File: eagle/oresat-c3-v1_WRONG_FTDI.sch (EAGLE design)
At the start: 168 parts, among them J1 J-SAMTEC-TFM-110-X1-XXX-D-RA, J10 U.FL, J11 U.FL, J13 U.FL, J14 U.FL, J15 HARWIN-2X8X1.27, J19 HARWIN-2X8X1.27, J2 U.FL, J3 U.FL, J4 U.FL, J6 J-SAMTEC-TFM-120-X1-XXX-D-RA, J7 FTSH-105-XX-X-DV-K, J8 U.FL, J9 U.FL, Q1 MOSFET-PCH-SOT23-6, U1 MAX892LEUA+T21-0036K-L, U11 U-ONSEMI-AX5043, U12 LP2985XX-N, U13 U-ONSEMI-AX5043, U14 LP2985XX-N, U2 TCAN330, U3 TCAN330, U4 TPS259621 - eFuse, U5 TPS62111RSA, U6 MAX6374KA-T21-0078H-L, U7 STM32F446RE, U9 SFEM016GB1EM1TO-A-HG-111-STD, X1 16MHZ-2.5x2mm, X3 TAITIEN-TY, X4 TAITIEN-TY

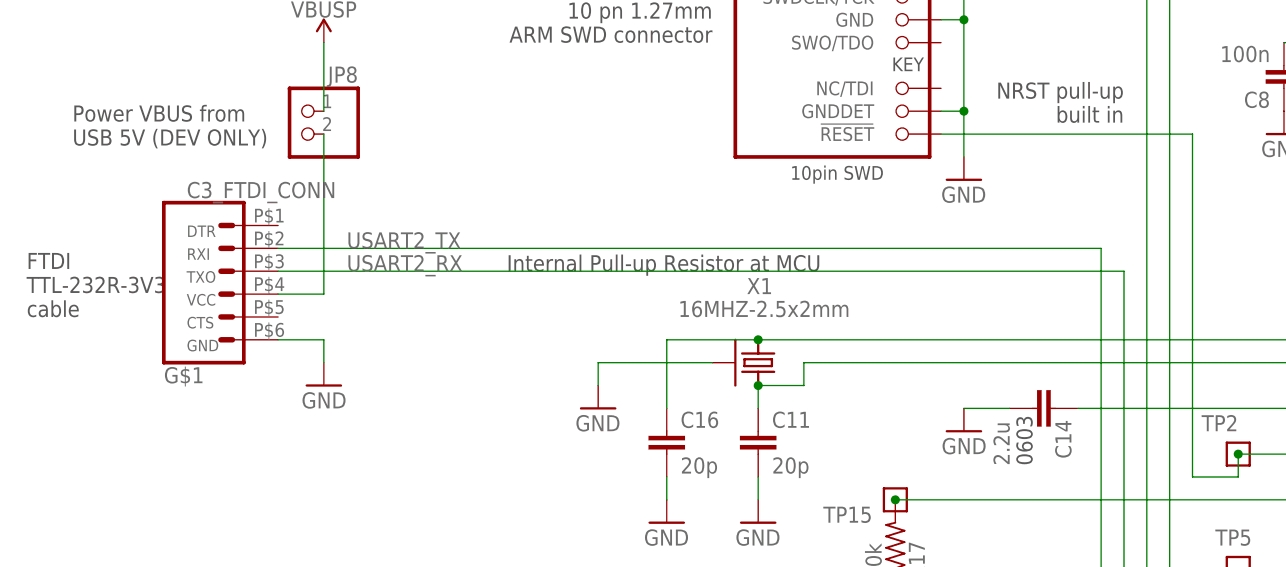
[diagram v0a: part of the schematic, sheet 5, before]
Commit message: switched the TX and RX pins to be the correct way
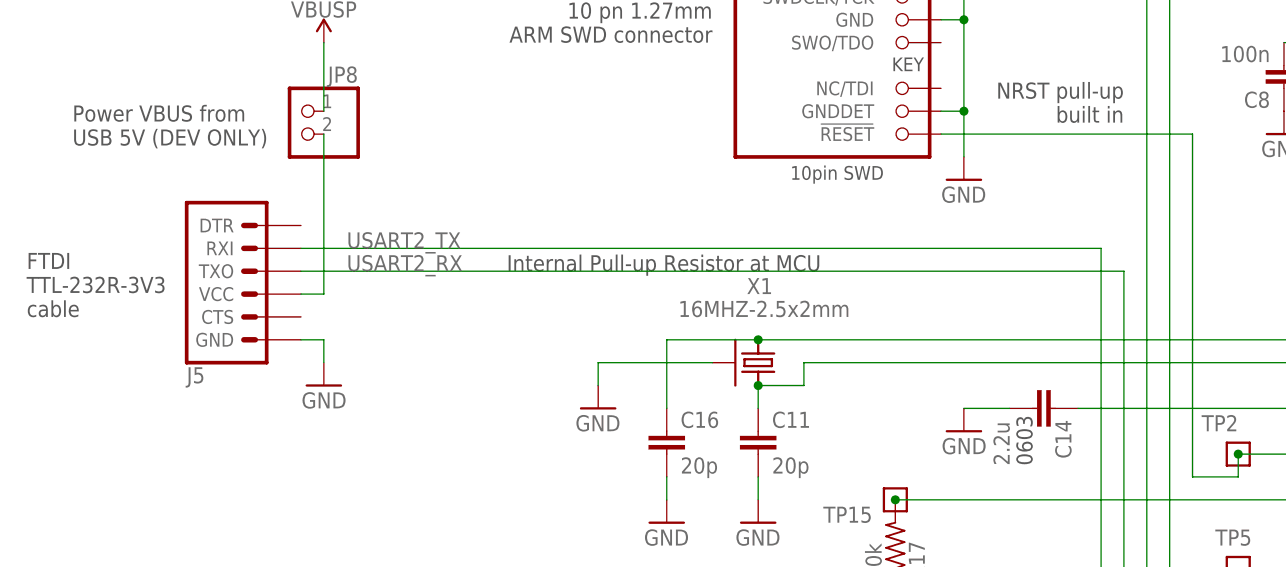
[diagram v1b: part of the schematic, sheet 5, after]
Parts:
- removed U$2: C3_FTDI_CONN, TrueC3_FTDIlbr:C3_FTDI_CONN
- added J5: (no value), SparkFun-Connectors:6_PIN_SERIAL_TARGETSILK
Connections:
- net GND: now also J5.GND; no longer U$2.GND
- net N$406: now also J5.VCC; no longer U$2.VCC
- net USART2_RX: now also J5.TXO; no longer U$2.TXO
- net USART2_TX: now also J5.RXI; no longer U$2.RXI
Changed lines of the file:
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@@
 <part name="GND27" library="supply1" library_urn="urn:adsk.eagle:library:371" deviceset="GND" device=""/>
 <part name="GND30" library="supply1" library_urn="urn:adsk.eagle:library:371" deviceset="GND" device=""/>
+<part name="J5" library="SparkFun-Connectors" library_urn="urn:adsk.eagle:library:513" deviceset="6_PIN_SERIAL_TARGET" device="SILK" package3d_urn="urn:adsk.eagle:package:37995/1"/>
 <part name="GND6" library="supply1" library_urn="urn:adsk.eagle:library:371" deviceset="GND" device=""/>
 <part name="H1" library="SparkFun-Hardware" library_urn="urn:adsk.eagle:library:519" deviceset="STAND-OFF" device="TIGHT" package3d_urn="urn:adsk.eagle:package:38629/1"/>
@@
 <part name="TP9" library="Tova" deviceset="TEST-POINT" device=""/>
 <part name="TP11" library="Tova" deviceset="TEST-POINT" device=""/>
-<part name="U$2" library="TrueC3_FTDIlbr" deviceset="C3_FTDI_CONN" device=""/>
 </parts>
 <sheets>
@@
 <attribute name="VALUE" x="316.23" y="219.71" size="1.778" layer="96" rot="MR90"/>
 </instance>
+<instance part="J5" gate="G$1" x="68.58" y="160.02" smashed="yes" rot="MR180">
+<attribute name="VALUE" x="60.96" y="169.926" size="1.778" layer="96" font="vector" rot="MR180"/>
+<attribute name="NAME" x="60.96" y="149.352" size="1.778" layer="95" font="vector" rot="MR180"/>
+</instance>
 <instance part="GND6" gate="1" x="76.2" y="147.32" smashed="yes" rot="MR0">
 <attribute name="VALUE" x="78.74" y="144.78" size="1.778" layer="96" rot="MR0"/>
@@
 <attribute name="NAME" x="411.48" y="43.18" size="1.778" layer="95" font="vector" rot="MR0"/>
 </instance>
-<instance part="U$2" gate="G$1" x="66.04" y="160.02" smashed="yes" rot="MR180">
-<attribute name="VALUE" x="60.96" y="169.926" size="1.778" layer="96" font="vector" rot="MR180"/>
-</instance>
 </instances>
 <busses>
@@
 </segment>
 <segment>
+<pinref part="J5" gate="G$1" pin="GND"/>
 <pinref part="GND6" gate="1" pin="GND"/>
-<wire x1="71.12" y1="152.4" x2="76.2" y2="152.4" width="0.1524" layer="91"/>
+<wire x1="73.66" y1="152.4" x2="76.2" y2="152.4" width="0.1524" layer="91"/>
 <wire x1="76.2" y1="152.4" x2="76.2" y2="149.86" width="0.1524" layer="91"/>
-<pinref part="U$2" gate="G$1" pin="GND"/>
 </segment>
 <segment>
@@
 <label x="78.74" y="162.56" size="1.778" layer="95"/>
 <pinref part="U7" gate="G$1" pin="PA2"/>
-<wire x1="162.56" y1="162.56" x2="71.12" y2="162.56" width="0.1524" layer="91"/>
-<pinref part="U$2" gate="G$1" pin="RXI"/>
+<pinref part="J5" gate="G$1" pin="RXI"/>
+<wire x1="162.56" y1="162.56" x2="73.66" y2="162.56" width="0.1524" layer="91"/>
 </segment>
 </net>
@@
 <label x="78.74" y="160.02" size="1.778" layer="95"/>
 <pinref part="U7" gate="G$1" pin="PA3"/>
-<wire x1="71.12" y1="160.02" x2="165.1" y2="160.02" width="0.1524" layer="91"/>
-<pinref part="U$2" gate="G$1" pin="TXO"/>
+<pinref part="J5" gate="G$1" pin="TXO"/>
+<wire x1="73.66" y1="160.02" x2="165.1" y2="160.02" width="0.1524" layer="91"/>
 </segment>
 </net>
@@
 <net name="N$406" class="0">
 <segment>
+<pinref part="J5" gate="G$1" pin="VCC"/>
 <pinref part="JP8" gate="G$1" pin="2"/>
-<wire x1="71.12" y1="157.48" x2="76.2" y2="157.48" width="0.1524" layer="91"/>
+<wire x1="73.66" y1="157.48" x2="76.2" y2="157.48" width="0.1524" layer="91"/>
 <wire x1="76.2" y1="157.48" x2="76.2" y2="175.26" width="0.1524" layer="91"/>
-<pinref part="U$2" gate="G$1" pin="VCC"/>
 </segment>
 </net>
